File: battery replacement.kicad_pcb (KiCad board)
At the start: 2 copper layers, 22.5 x 11.1 mm, 15 parts, among them U1 GP3134_C48997205

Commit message: prelim. 10x25mm ~ 180pcs
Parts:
- removed R4: 10k, JLCImport:0402WGF1002TCE
- added C7: 4.7uF, JLCImport:CL21A475KAQNNNE, F.Cu at (139.6, 45.5)
- added U2: Y4203-ADJM6R, JLCImport:Y4203-ADJM6R, F.Cu at (139.7, 42.5)
- L1: value 4.7uH -> 470nH; footprint JLCImport:BMQA000606304R7MA1 -> JLCImport:TMS252012ALM-R47MTAA
- R1: value 10k -> 100k; footprint JLCImport:0402WGF1002TCE -> JLCImport:0402WGF1003TCE
- R2: value 20k -> 549k; footprint JLCImport:0402WGF2002TCE -> JLCImport:0402WGF5493TCE
- R3: value 20k -> 100k; footprint JLCImport:0402WGF2002TCE -> JLCImport:0402WGF1003TCE
- U1: value GP3134_C48997205 -> RT5788BGJ8F; footprint JLCImport:GP3134_C48997205 -> JLCImport:RT5788BGJ8F
- moved TP2 35.0 mm to (127.8, 47.0)
- moved TP1 34.8 mm to (127.8, 39.0)
- moved C4 29.1 mm to (128.1, 42.9)
- moved C3 29.0 mm to (130.6, 43.6)
- moved C2 27.9 mm to (137.0, 41.2), turned to 0 degrees
- moved U1 27.4 mm to (134.4, 42.9)
- moved L1 23.5 mm to (132.0, 39.5), turned to 180 degrees
- moved C1 22.8 mm to (139.0, 39.4), turned to 180 degrees
- moved R2 21.9 mm to (132.5, 45.7), turned to 90 degrees
- moved R3 16.1 mm to (137.1, 42.9), turned to 90 degrees
- moved R1 15.2 mm to (133.8, 45.7)
- moved R5 14.9 mm to (146.7, 47.2)
- moved R6 12.3 mm to (149.2, 46.6)
- moved USB1 8.66 mm to (146.6, 43.0), turned to 180 degrees
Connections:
- C1 pad 1: +5V -> GND
- C1 pad 2: GND -> +5V
- C2 pad 1: /SW -> +5V
- C2 pad 2: /BS -> GND
- C3 pad 2: /V_OUT -> /VOUT
- C4 pad 2: /V_OUT -> /VOUT
- L1 pad 1: /SW -> /LX
- L1 pad 2: /V_OUT -> /VOUT
- R1 pad 1: /EN -> /FB
- R1 pad 2: +5V -> /AGND
- R2 pad 1: Net-(R2-Pad1) -> /FB
- R2 pad 2: /V_OUT -> /VOUT
- R3 pad 1: /FB -> /EN
- R3 pad 2: Net-(R2-Pad1) -> +5V
- TP1 pad 1: /V_OUT -> /VOUT
- U1 pad 1: GND -> unconnected-(U1-PGOOD-Pad1)
- U1 pad 2: /SW -> +5V
- U1 pad 3: +5V -> /LX
- U1 pad 4: /FB -> /PGND
- U1 pad 5: /EN -> /VOUT
- U1 pad 6: /BS -> /AGND
- USB1 pad A9: +5V -> /VBUS
- USB1 pad B9: +5V -> /VBUS
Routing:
- net +5V: track 20.2 -> 0.00 mm
- net Net-(USB1-CC1): track 18.4 -> 0.00 mm, vias 2 -> 0
- net /FB: track 18.0 -> 0.00 mm, vias 2 -> 0
- net Net-(USB1-CC2): track 17.9 -> 0.00 mm, vias 2 -> 0
- net /EN: track 17.7 -> 0.00 mm, vias 2 -> 0
- net /V_OUT: track 11.0 -> 0.00 mm
- net /SW: track 10.6 -> 0.00 mm
- net GND: track 4.17 -> 0.00 mm, vias 28 -> 0
- net /BS: track 1.66 -> 0.00 mm
- net Net-(R2-Pad1): track 1.27 -> 0.00 mm
- removed copper zone on B.Cu, net GND
- removed copper zone on F.Cu, net GND
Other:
- board size 22.5 x 11.1 mm -> 25 x 10 mm

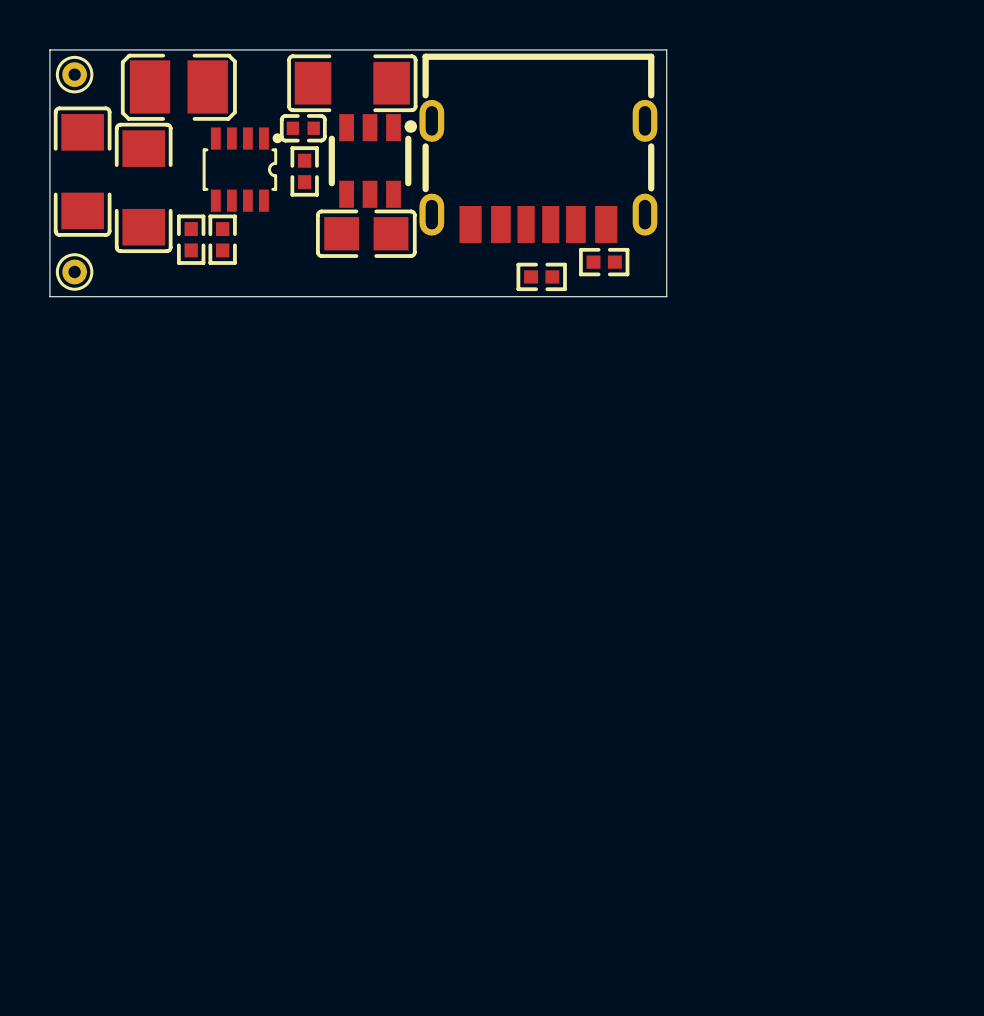
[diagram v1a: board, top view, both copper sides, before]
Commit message: prelim 9x25mm ~ 200pcs
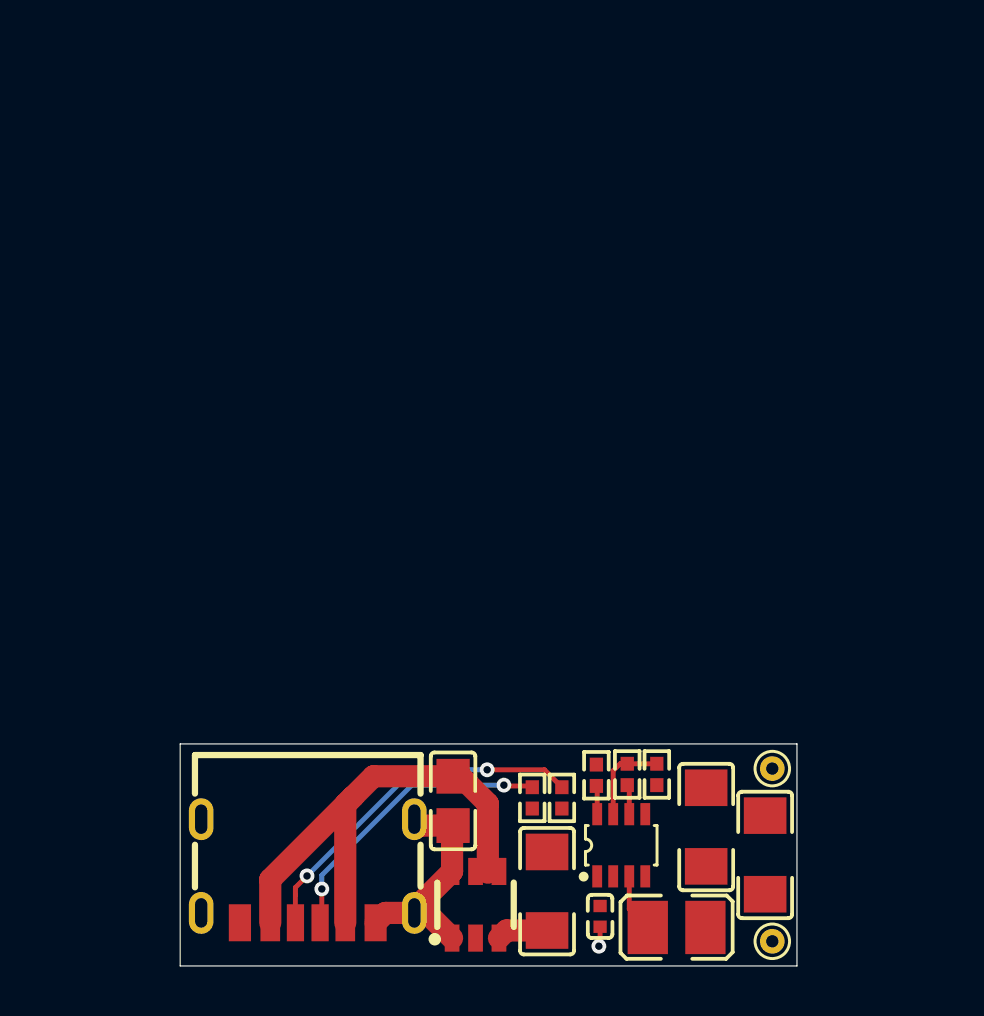
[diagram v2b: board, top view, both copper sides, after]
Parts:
- moved TP1 45.1 mm to (156.0, 74.1)
- moved L1 39.6 mm to (152.2, 73.6), turned to 0 degrees
- moved C4 39.1 mm to (155.7, 70.6), turned to -90 degrees
- moved TP2 34.7 mm to (156.0, 67.1)
- moved C3 34.5 mm to (153.3, 69.5), turned to -90 degrees
- moved C2 34.1 mm to (149.1, 73.1), turned to -90 degrees
- moved C1 33.7 mm to (146.9, 72.1), turned to -90 degrees
- moved U1 31.4 mm to (149.9, 70.2), turned to 0 degrees
- moved U2 30.5 mm to (144.0, 72.7), turned to -90 degrees
- moved USB1 29.8 mm to (137.2, 71.3)
- moved R2 28.7 mm to (151.3, 67.4), turned to -90 degrees
- moved R3 27.2 mm to (148.9, 67.4)
- moved R1 27.2 mm to (150.2, 67.4), turned to -90 degrees
- moved C7 23.3 mm to (143.1, 68.4), turned to 90 degrees
- moved R6 21.9 mm to (146.3, 68.3), turned to -90 degrees
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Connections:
- R1 pad 2: /AGND -> GND
- U1 pad 4: /PGND -> GND
- U1 pad 6: /AGND -> GND
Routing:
- net /VBUS: track 0.00 -> 20.8 mm
- net Net-(USB1-CC1): track 0.00 -> 14.5 mm, vias 0 -> 2
- net Net-(USB1-CC2): track 0.00 -> 12.0 mm, vias 0 -> 2
- net GND: track 0.00 -> 11.6 mm, vias 0 -> 1
- net /FB: track 0.00 -> 3.65 mm
- net /LX: track 0.00 -> 2.38 mm
- net +5V: track 0.00 -> 2.08 mm
- net /EN: track 0.00 -> 1.16 mm
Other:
- board size 25 x 10 mm -> 25 x 9 mm

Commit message: kicad prelim version
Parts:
- moved C1 0.22 mm to (143.3, 68.4)
- moved USB1 0.17 mm to (137.4, 71.2)
- moved C4 0.12 mm to (153.3, 69.4)
- moved C3 0.10 mm to (148.9, 73.1)
- moved R3 0.09 mm to (149.0, 67.3)
- moved L1 0.09 mm to (152.1, 73.5)
- moved C5 0.06 mm to (155.7, 70.6)
- renumbered C7 to C1, C1 to C2, C2 to C3, C3 to C4, C4 to C5, R5 to R1, R6 to R2, R2 to R4, R1 to R5, U2 to U1, U1 to U2
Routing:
- net GND: track 11.6 -> 1.21 mm, vias 1 -> 18
- net +5V: track 2.08 -> 7.78 mm
- net /VOUT: track 0.00 -> 5.05 mm
- net /LX: track 2.38 -> 0.00 mm
- net Net-(USB1-CC1): track 14.5 -> 15.6 mm
- net Net-(USB1-CC2): track 12.0 -> 13.0 mm
- added copper zone on B.Cu, net GND
- added copper zone on F.Cu, net GND
